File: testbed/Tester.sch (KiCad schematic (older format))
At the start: 11 parts, among them SW00 SW_PUSH, SW01 SW_PUSH, SW10 SW_PUSH, SW11 SW_PUSH, U1 ATmega32U4

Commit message: Added annotation to tenter sheet.
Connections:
- net labels added: 20170208, ApotheonPwnxorProofOfConcept
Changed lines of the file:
@@
 LIBS:contrib
 LIBS:valves
+LIBS:Tester-cache
 EELAYER 25 0
 EELAYER END
@@
 Wire Wire Line
 	7550 3150 7600 3150
+Text Label 7350 7500 0    60   ~ 0
+ApotheonPwnxorProofOfConcept
+Text Label 8150 7650 0    60   ~ 0
+20170208
 $EndSCHEMATC

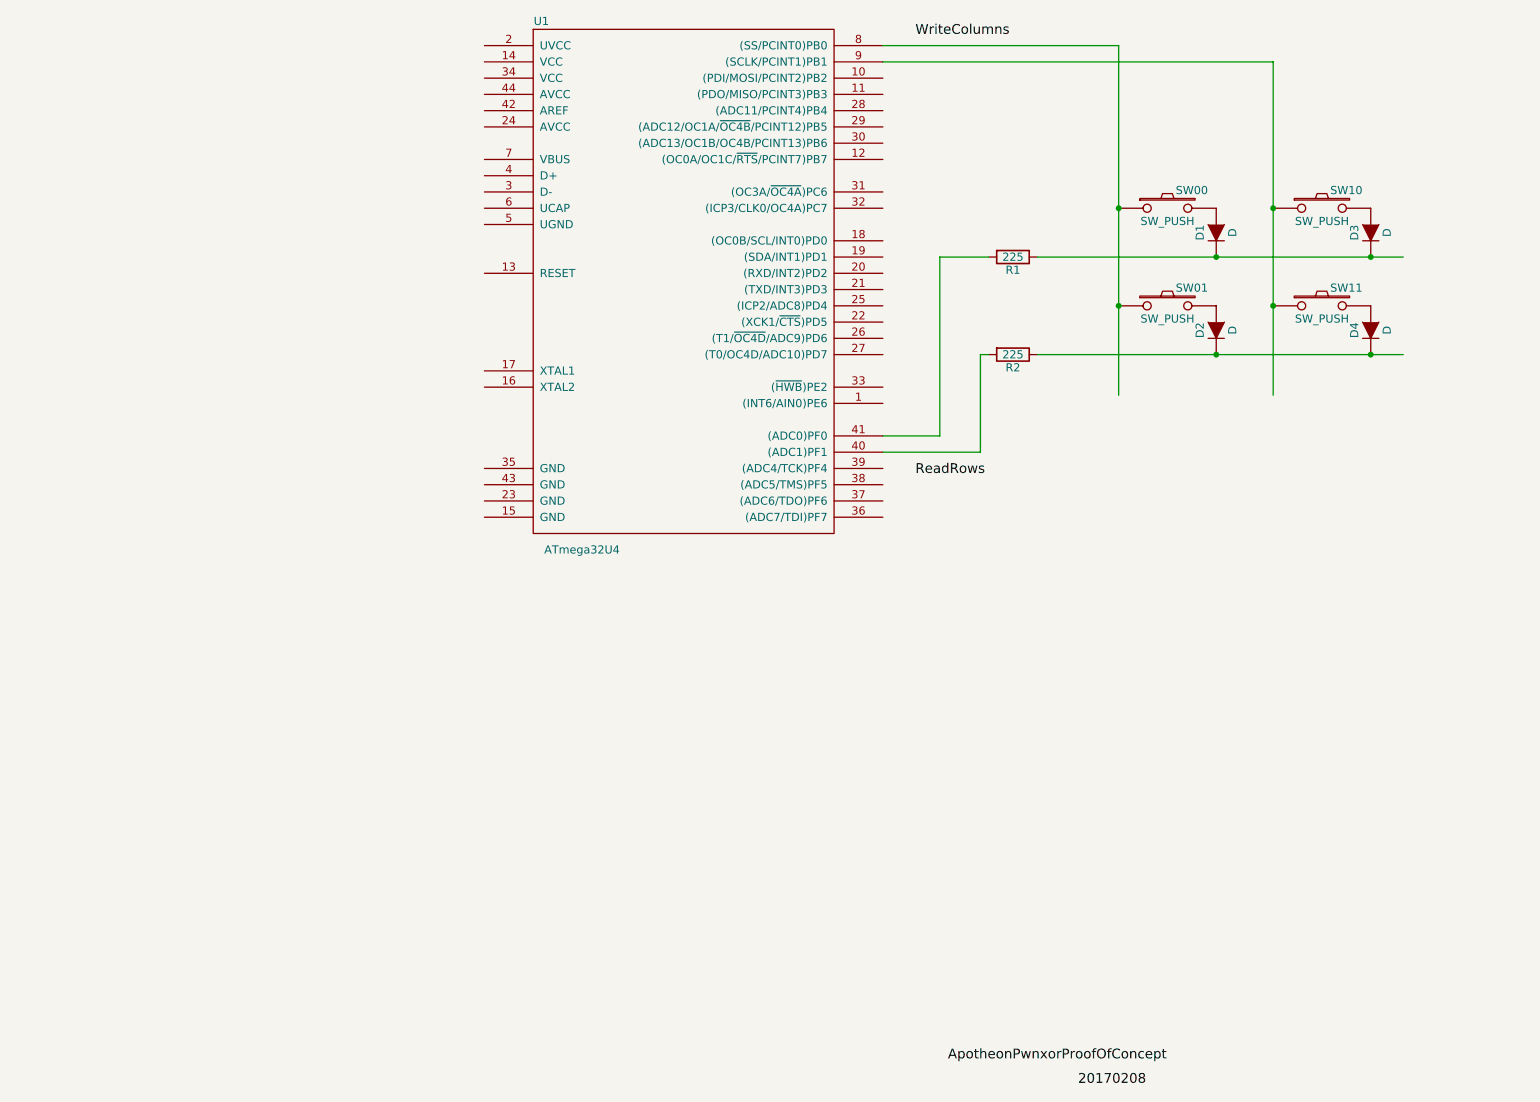
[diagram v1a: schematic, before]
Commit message: Added LEDs for testing.
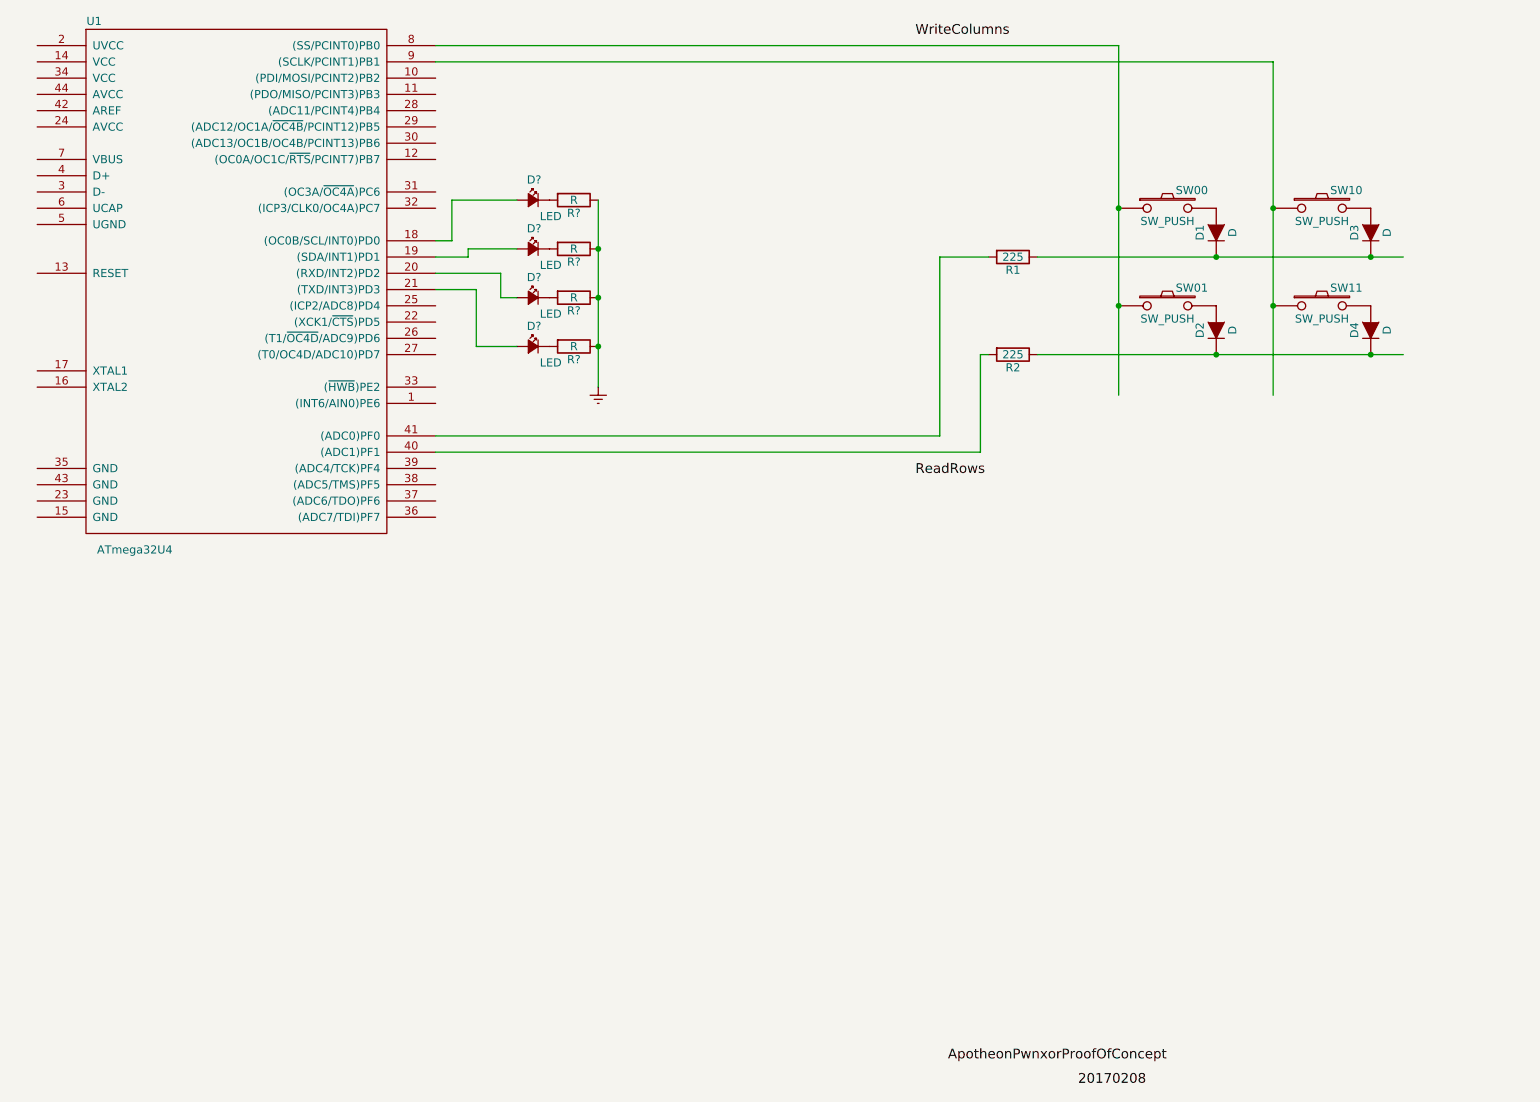
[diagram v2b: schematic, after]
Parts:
- added D? (x4): LED, symbol Led_Small
- added R? (x4): R, symbol R
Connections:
- net labels added: Earth
- wire segments 12 -> 25
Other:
- moved on the sheet: U1
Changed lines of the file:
@@
 L ATmega32U4 U1
 U 1 1 589ADD6D
-P 5750 2800
-F 0 "U1" H 4850 4500 50  0000 C CNN
-F 1 "ATmega32U4" H 5100 1250 50  0000 C CNN
-F 2 "" H 6950 3900 50  0000 C CNN
-F 3 "" H 6950 3900 50  0000 C CNN
-	1    5750 2800
+P 3000 2800
+F 0 "U1" H 2100 4500 50  0000 C CNN
+F 1 "ATmega32U4" H 2350 1250 50  0000 C CNN
+F 2 "" H 4200 3900 50  0000 C CNN
+F 3 "" H 4200 3900 50  0000 C CNN
+	1    3000 2800
 	1    0    0    -1
 $EndComp
 Wire Wire Line
-	6950 1250 8400 1250
+	4200 1250 8400 1250
 Wire Wire Line
-	6950 1350 9350 1350
+	4200 1350 9350 1350
 Wire Wire Line
 	7550 3150 7550 3750
 Wire Wire Line
-	7550 3750 6950 3750
+	7550 3750 4200 3750
 Wire Wire Line
 	7300 2550 7300 3650
 Wire Wire Line
-	7300 3650 6950 3650
+	7300 3650 4200 3650
 Text Label 7150 1200 0    60   ~ 0
 WriteColumns
@@
 Text Label 8150 7650 0    60   ~ 0
 20170208
+$Comp
+L Led_Small D?
+U 1 1 590FD51F
+P 4800 2200
+F 0 "D?" H 4750 2325 50  0000 L CNN
+F 1 "LED" H 4625 2100 50  0000 L CNN
+F 2 "" V 4800 2200 50  0000 C CNN
+F 3 "" V 4800 2200 50  0000 C CNN
+	1    4800 2200
+	-1   0    0    -1
+$EndComp
+$Comp
+L R R?
+U 1 1 590FD67F
+P 5050 2200
+F 0 "R?" V 5130 2200 50  0000 C CNN
+F 1 "R" V 5050 2200 50  0000 C CNN
+F 2 "" V 4980 2200 50  0000 C CNN
+F 3 "" H 5050 2200 50  0000 C CNN
+	1    5050 2200
+	0    1    1    0
+$EndComp
+$Comp
+L Led_Small D?
+U 1 1 590FE73A
+P 4800 2500
+F 0 "D?" H 4750 2625 50  0000 L CNN
+F 1 "LED" H 4625 2400 50  0000 L CNN
+F 2 "" V 4800 2500 50  0000 C CNN
+F 3 "" V 4800 2500 50  0000 C CNN
+	1    4800 2500
+	-1   0    0    -1
+$EndComp
+$Comp
+L R R?
+U 1 1 590FE741
+P 5050 2500
+F 0 "R?" V 5130 2500 50  0000 C CNN
+F 1 "R" V 5050 2500 50  0000 C CNN
+F 2 "" V 4980 2500 50  0000 C CNN
+F 3 "" H 5050 2500 50  0000 C CNN
+	1    5050 2500
+	0    1    1    0
+$EndComp
+$Comp
+L Led_Small D?
+U 1 1 590FE839
+P 4800 2800
+F 0 "D?" H 4750 2925 50  0000 L CNN
+F 1 "LED" H 4625 2700 50  0000 L CNN
+F 2 "" V 4800 2800 50  0000 C CNN
+F 3 "" V 4800 2800 50  0000 C CNN
+	1    4800 2800
+	-1   0    0    -1
+$EndComp
+$Comp
+L R R?
+U 1 1 590FE840
+P 5050 2800
+F 0 "R?" V 5130 2800 50  0000 C CNN
+F 1 "R" V 5050 2800 50  0000 C CNN
+F 2 "" V 4980 2800 50  0000 C CNN
+F 3 "" H 5050 2800 50  0000 C CNN
+	1    5050 2800
+	0    1    1    0
+$EndComp
+$Comp
+L Led_Small D?
+U 1 1 590FE914
+P 4800 3100
+F 0 "D?" H 4750 3225 50  0000 L CNN
+F 1 "LED" H 4625 3000 50  0000 L CNN
+F 2 "" V 4800 3100 50  0000 C CNN
+F 3 "" V 4800 3100 50  0000 C CNN
+	1    4800 3100
+	-1   0    0    -1
+$EndComp
+$Comp
+L R R?
+U 1 1 590FE91B
+P 5050 3100
+F 0 "R?" V 5130 3100 50  0000 C CNN
+F 1 "R" V 5050 3100 50  0000 C CNN
+F 2 "" V 4980 3100 50  0000 C CNN
+F 3 "" H 5050 3100 50  0000 C CNN
+	1    5050 3100
+	0    1    1    0
+$EndComp
+Wire Wire Line
+	5200 2200 5200 3350
+$Comp
+L Earth #PWR?
+U 1 1 590FF2FC
+P 5200 3350
+F 0 "#PWR?" H 5200 3100 50  0001 C CNN
+F 1 "Earth" H 5200 3200 50  0001 C CNN
+F 2 "" H 5200 3350 50  0000 C CNN
+F 3 "" H 5200 3350 50  0000 C CNN
+	1    5200 3350
+	1    0    0    -1
+$EndComp
+Connection ~ 5200 2500
+Connection ~ 5200 2800
+Connection ~ 5200 3100
+Wire Wire Line
+	4200 2450 4300 2450
+Wire Wire Line
+	4300 2450 4300 2200
+Wire Wire Line
+	4300 2200 4700 2200
+Wire Wire Line
+	4200 2550 4400 2550
+Wire Wire Line
+	4400 2550 4400 2500
+Wire Wire Line
+	4400 2500 4700 2500
+Wire Wire Line
+	4200 2650 4600 2650
+Wire Wire Line
+	4600 2650 4600 2800
+Wire Wire Line
+	4600 2800 4700 2800
+Wire Wire Line
+	4200 2750 4450 2750
+Wire Wire Line
+	4450 2750 4450 3100
+Wire Wire Line
+	4450 3100 4700 3100
 $EndSCHEMATC

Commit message: Update labels
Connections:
- net labels added: 20170512
- net labels removed: 20170208
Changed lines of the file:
@@
 ApotheonPwnxorProofOfConcept
 Text Label 8150 7650 0    60   ~ 0
-20170208
+20170512
 $Comp
 L Led_Small D?

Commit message: Updated to actual build. V 0.0.0
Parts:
- R1, R2: value 225 -> 100
- R3, R4, R5, R6: renamed from R?; value R -> 150
- gave numbers to parts that had none: 4
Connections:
- net labels added: 20170512a
- net labels removed: 20170512, Earth
- wire segments 25 -> 28
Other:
- note added: "0.0.0"
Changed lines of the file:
@@
 P 7750 2550
 F 0 "R1" V 7830 2550 50  0000 C CNN
-F 1 "225" V 7750 2550 50  0000 C CNN
+F 1 "100" V 7750 2550 50  0000 C CNN
 F 2 "" V 7680 2550 50  0000 C CNN
 F 3 "" H 7750 2550 50  0000 C CNN
@@
 P 7750 3150
 F 0 "R2" V 7830 3150 50  0000 C CNN
-F 1 "225" V 7750 3150 50  0000 C CNN
+F 1 "100" V 7750 3150 50  0000 C CNN
 F 2 "" V 7680 3150 50  0000 C CNN
 F 3 "" H 7750 3150 50  0000 C CNN
@@
 ApotheonPwnxorProofOfConcept
 Text Label 8150 7650 0    60   ~ 0
-20170512
+20170512a
 $Comp
-L Led_Small D?
+L Led_Small D3
 U 1 1 590FD51F
 P 4800 2200
-F 0 "D?" H 4750 2325 50  0000 L CNN
+F 0 "D3" H 4750 2325 50  0000 L CNN
 F 1 "LED" H 4625 2100 50  0000 L CNN
 F 2 "" V 4800 2200 50  0000 C CNN
@@
 $EndComp
 $Comp
-L R R?
+L R R3
 U 1 1 590FD67F
 P 5050 2200
-F 0 "R?" V 5130 2200 50  0000 C CNN
-F 1 "R" V 5050 2200 50  0000 C CNN
+F 0 "R3" V 5130 2200 50  0000 C CNN
+F 1 "150" V 5050 2200 50  0000 C CNN
 F 2 "" V 4980 2200 50  0000 C CNN
 F 3 "" H 5050 2200 50  0000 C CNN
@@
 $EndComp
 $Comp
-L Led_Small D?
+L Led_Small D4
 U 1 1 590FE73A
 P 4800 2500
-F 0 "D?" H 4750 2625 50  0000 L CNN
+F 0 "D4" H 4750 2625 50  0000 L CNN
 F 1 "LED" H 4625 2400 50  0000 L CNN
 F 2 "" V 4800 2500 50  0000 C CNN
@@
 $EndComp
 $Comp
-L R R?
+L R R4
 U 1 1 590FE741
 P 5050 2500
-F 0 "R?" V 5130 2500 50  0000 C CNN
-F 1 "R" V 5050 2500 50  0000 C CNN
+F 0 "R4" V 5130 2500 50  0000 C CNN
+F 1 "150" V 5050 2500 50  0000 C CNN
 F 2 "" V 4980 2500 50  0000 C CNN
 F 3 "" H 5050 2500 50  0000 C CNN
@@
 $EndComp
 $Comp
-L Led_Small D?
+L Led_Small D5
 U 1 1 590FE839
 P 4800 2800
-F 0 "D?" H 4750 2925 50  0000 L CNN
+F 0 "D5" H 4750 2925 50  0000 L CNN
 F 1 "LED" H 4625 2700 50  0000 L CNN
 F 2 "" V 4800 2800 50  0000 C CNN
@@
 $EndComp
 $Comp
-L R R?
+L R R5
 U 1 1 590FE840
 P 5050 2800
-F 0 "R?" V 5130 2800 50  0000 C CNN
-F 1 "R" V 5050 2800 50  0000 C CNN
+F 0 "R5" V 5130 2800 50  0000 C CNN
+F 1 "150" V 5050 2800 50  0000 C CNN
 F 2 "" V 4980 2800 50  0000 C CNN
 F 3 "" H 5050 2800 50  0000 C CNN
@@
 $EndComp
 $Comp
-L Led_Small D?
+L Led_Small D6
 U 1 1 590FE914
 P 4800 3100
-F 0 "D?" H 4750 3225 50  0000 L CNN
+F 0 "D6" H 4750 3225 50  0000 L CNN
 F 1 "LED" H 4625 3000 50  0000 L CNN
 F 2 "" V 4800 3100 50  0000 C CNN
@@
 $EndComp
 $Comp
-L R R?
+L R R6
 U 1 1 590FE91B
 P 5050 3100
-F 0 "R?" V 5130 3100 50  0000 C CNN
-F 1 "R" V 5050 3100 50  0000 C CNN
+F 0 "R6" V 5130 3100 50  0000 C CNN
+F 1 "150" V 5050 3100 50  0000 C CNN
 F 2 "" V 4980 3100 50  0000 C CNN
 F 3 "" H 5050 3100 50  0000 C CNN
@@
 $EndComp
 Wire Wire Line
-	5200 2200 5200 3350
-$Comp
-L Earth #PWR?
-U 1 1 590FF2FC
-P 5200 3350
-F 0 "#PWR?" H 5200 3100 50  0001 C CNN
-F 1 "Earth" H 5200 3200 50  0001 C CNN
-F 2 "" H 5200 3350 50  0000 C CNN
-F 3 "" H 5200 3350 50  0000 C CNN
-	1    5200 3350
-	1    0    0    -1
-$EndComp
+	5200 2200 5200 4450
 Connection ~ 5200 2500
 Connection ~ 5200 2800
@@
 Wire Wire Line
 	4450 3100 4700 3100
+Wire Wire Line
+	1600 4450 5200 4450
+Wire Wire Line
+	1600 4150 1600 4450
+Wire Wire Line
+	1600 4150 1750 4150
+Text Notes 10600 7650 0    60   ~ 0
+0.0.0
 $EndSCHEMATC
